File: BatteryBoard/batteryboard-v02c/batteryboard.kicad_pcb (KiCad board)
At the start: 4 copper layers, 95.9 x 90.2 mm, 40 parts, among them J1 KEYSTONE-1042, J2 KEYSTONE-1042, J3 KEYSTONE-1042, J4 KEYSTONE-1042, J5 KEYSTONE-1042, J6 KEYSTONE-1042, J7 MOLEX 502352-0801, J8 1985807, Q1 IRF7458, Q2 IRF7458, Q3 DMP2040USS-13, Q4 IRLML2803, U1 R5460N233AF

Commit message: changed flags
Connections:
- net PyCubed_AIN5 renamed PyCubed_SENSE
- net PyCubed_HIN renamed PyCubed_ENABLE
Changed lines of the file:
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@@
 	(net 6 "Net-(U1-VC)")
 	(net 7 "Net-(C3-Pad1)")
-	(net 8 "PyCubed_AIN5")
+	(net 8 "PyCubed_SENSE")
 	(net 9 "unconnected-(H1-Pad1)")
 	(net 10 "Net-(U1-V-)")
@@
 	(net 17 "Net-(Q2-G)")
 	(net 18 "/HEATER")
-	(net 19 "PyCubed_HIN")
+	(net 19 "PyCubed_ENABLE")
 	(net 20 "Net-(Q4-G)")
 	(net 21 "PYCUBED_GND")
@@
 			(layers "F.Cu" "F.Paste" "F.Mask")
 			(roundrect_rratio 0.25)
-			(net 8 "PyCubed_AIN5")
+			(net 8 "PyCubed_SENSE")
 			(pintype "passive")
 		)
@@
 			(layers "*.Cu" "*.Mask")
 			(remove_unused_layers no)
-			(net 8 "PyCubed_AIN5")
+			(net 8 "PyCubed_SENSE")
 			(pintype "passive")
 		)
@@
 			(layers "F.Cu" "F.Paste" "F.Mask")
 			(roundrect_rratio 0.25)
-			(net 19 "PyCubed_HIN")
+			(net 19 "PyCubed_ENABLE")
 			(pintype "passive")
 		)
@@
 			(size 1.2446 3.2512)
 			(layers "F.Cu" "F.Paste" "F.Mask")
-			(net 19 "PyCubed_HIN")
+			(net 19 "PyCubed_ENABLE")
 			(pinfunction "5")
 			(pintype "passive")
@@
 			(size 1.2446 3.2512)
 			(layers "F.Cu" "F.Paste" "F.Mask")
-			(net 8 "PyCubed_AIN5")
+			(net 8 "PyCubed_SENSE")
 			(pinfunction "6")
 			(pintype "passive")

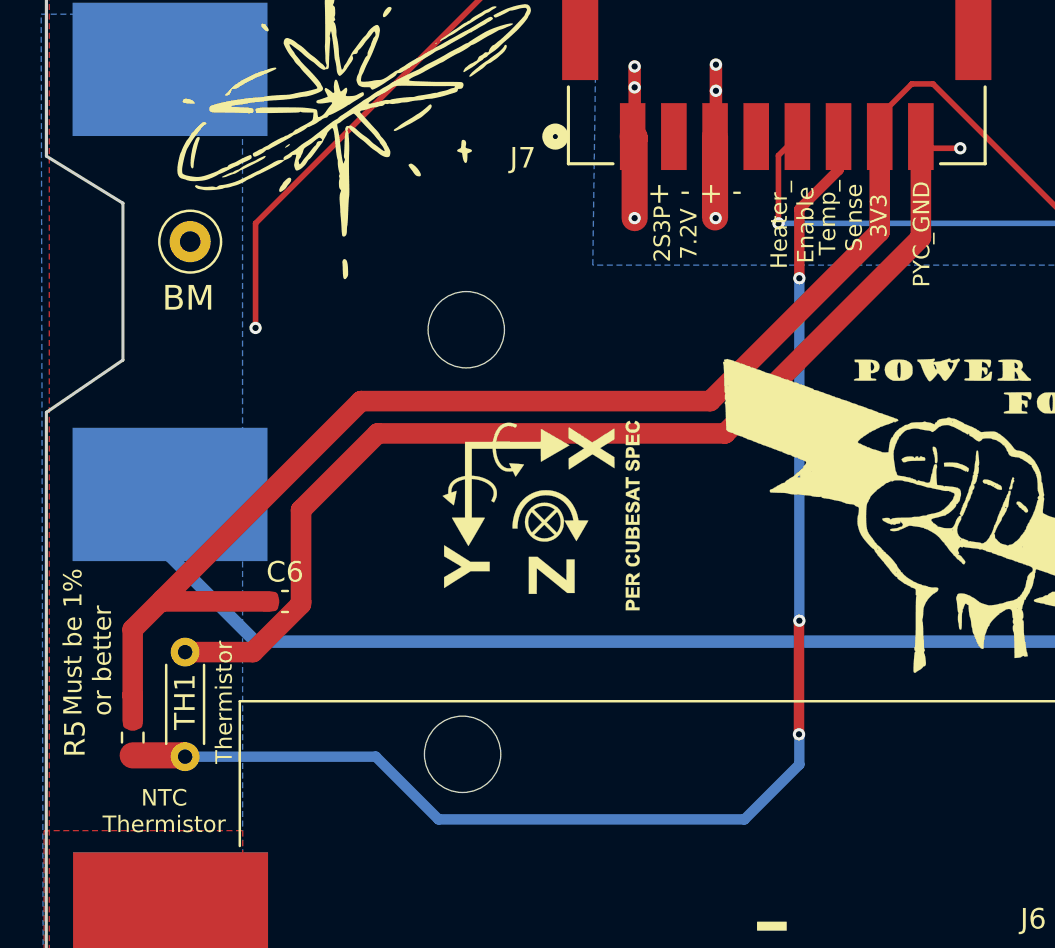
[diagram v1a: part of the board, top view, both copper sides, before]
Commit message: fixed traces on thermistor circuit
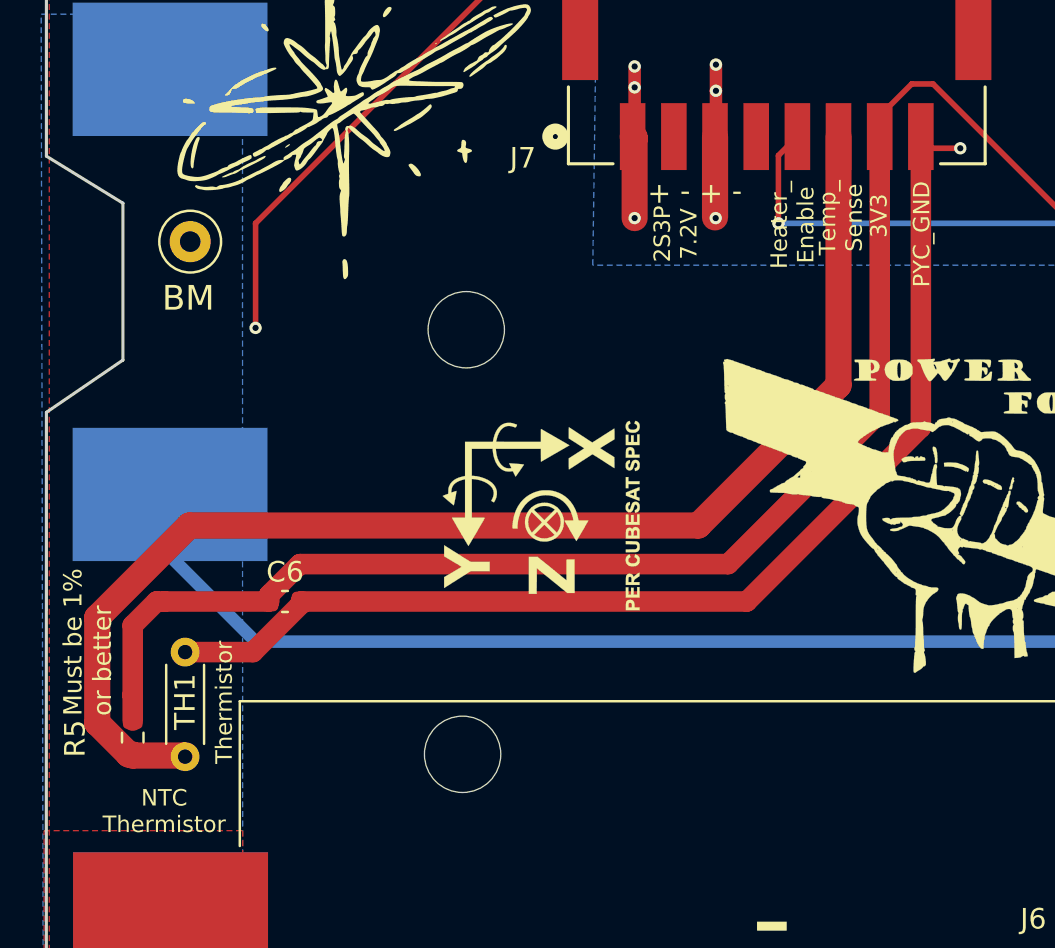
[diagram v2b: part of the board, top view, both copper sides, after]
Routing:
- net PYCUBED_GND: track 140.0 -> 142.8 mm
- net PyCubed_SENSE: track 65.6 -> 62.8 mm, vias 3 -> 0
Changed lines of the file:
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@@
 	(segment
 		(start 57.3913 101.2464)
-		(end 59.8778 101.2464)
+		(end 57.3988 101.2539)
 		(width 1.27)
 		(layer "F.Cu")
@@
 	)
 	(segment
-		(start 89.7763 74.715499)
-		(end 91.680299 72.8115)
-		(width 0.508)
+		(start 57.3988 101.2539)
+		(end 59.8853 101.2539)
+		(width 1.27)
 		(layer "F.Cu")
 		(net 8)
 	)
 	(segment
-		(start 59.8778 101.2464)
-		(end 59.9393 101.3079)
+		(start 91.680299 71.1859)
+		(end 91.680299 83.268301)
 		(width 1.27)
 		(layer "F.Cu")
@@
 	)
 	(segment
-		(start 91.680299 72.8115)
-		(end 91.680299 71.1859)
-		(width 0.508)
+		(start 59.8853 101.2539)
+		(end 59.9393 101.3079)
+		(width 1.27)
 		(layer "F.Cu")
 		(net 8)
 	)
 	(segment
-		(start 89.7599 94.7203)
-		(end 89.7763 94.7039)
-		(width 0.508)
+		(start 84.8697 90.0789)
+		(end 60.141876 90.0789)
+		(width 1.27)
 		(layer "F.Cu")
 		(net 8)
 	)
 	(segment
-		(start 89.7599 100.2215)
-		(end 89.7599 94.7203)
-		(width 0.508)
+		(start 55.6697 99.669914)
+		(end 57.203686 101.2039)
+		(width 1.27)
 		(layer "F.Cu")
 		(net 8)
 	)
 	(segment
-		(start 89.7763 78.0669)
-		(end 89.7763 74.715499)
-		(width 0.508)
+		(start 60.141876 90.0789)
+		(end 55.6697 94.551076)
+		(width 1.27)
 		(layer "F.Cu")
 		(net 8)
 	)
-	(via
-		(at 89.7763 78.0669)
-		(size 0.6)
-		(drill 0.3)
-		(layers "F.Cu" "B.Cu")
-		(net 8)
-	)
-	(via
-		(at 89.7599 100.2215)
-		(size 0.6)
-		(drill 0.3)
-		(layers "F.Cu" "B.Cu")
-		(net 8)
-	)
-	(via
-		(at 89.7763 94.7039)
-		(size 0.6)
-		(drill 0.3)
-		(layers "F.Cu" "B.Cu")
-		(net 8)
-	)
 	(segment
-		(start 89.7763 101.6889)
-		(end 89.7763 100.2379)
-		(width 0.508)
-		(layer "B.Cu")
-		(net 8)
-	)
-	(segment
-		(start 72.2503 104.3559)
-		(end 87.1093 104.3559)
-		(width 0.508)
-		(layer "B.Cu")
-		(net 8)
-	)
-	(segment
-		(start 69.2023 101.3079)
-		(end 72.2503 104.3559)
-		(width 0.508)
-		(layer "B.Cu")
-		(net 8)
-	)
-	(segment
-		(start 89.7763 94.7039)
-		(end 89.7763 78.0669)
-		(width 0.508)
-		(layer "B.Cu")
-		(net 8)
-	)
-	(segment
-		(start 60.4393 101.3079)
-		(end 69.2023 101.3079)
-		(width 0.508)
-		(layer "B.Cu")
+		(start 57.203686 101.2039)
+		(end 57.3947 101.2039)
+		(width 1.27)
+		(layer "F.Cu")
 		(net 8)
 	)
 	(segment
-		(start 89.7763 100.2379)
-		(end 89.7599 100.2215)
-		(width 0.508)
-		(layer "B.Cu")
+		(start 91.680299 83.268301)
+		(end 84.8697 90.0789)
+		(width 1.27)
+		(layer "F.Cu")
 		(net 8)
 	)
 	(segment
-		(start 87.1093 104.3559)
-		(end 89.7763 101.6889)
-		(width 0.508)
-		(layer "B.Cu")
+		(start 55.6697 94.551076)
+		(end 55.6697 99.669914)
+		(width 1.27)
+		(layer "F.Cu")
 		(net 8)
 	)
@@
 	)
 	(segment
-		(start 57.3947 98.3248)
-		(end 57.3947 99.5539)
-		(width 1)
-		(layer "F.Cu")
-		(net 15)
-	)
-	(segment
 		(start 109.68021 76.84999)
 		(end 111.36012 78.5299)
@@
 	)
 	(segment
-		(start 57.3913 98.3214)
-		(end 57.3913 95.1251)
+		(start 65.5197 91.9539)
+		(end 86.3197 91.9539)
 		(width 1)
 		(layer "F.Cu")
@@
 	)
 	(segment
-		(start 57.3913 98.3214)
-		(end 57.3947 98.3248)
+		(start 57.3947 98.3248)
+		(end 57.3913 98.3214)
+		(width 1)
+		(layer "F.Cu")
+		(net 15)
+	)
+	(segment
+		(start 64.0167 93.4569)
+		(end 65.5197 91.9539)
 		(width 1)
 		(layer "F.Cu")
@@
 	)
 	(segment
-		(start 109.68021 76.84999)
-		(end 111.6103 74.9199)
-		(width 0.27178)
+		(start 58.5537 93.7699)
+		(end 58.9497 93.7699)
+		(width 1)
 		(layer "F.Cu")
 		(net 15)
 	)
 	(segment
-		(start 93.6803 75.8033)
-		(end 93.6803 71.1859)
+		(start 86.3197 91.9539)
+		(end 93.6803 84.5933)
 		(width 1)
 		(layer "F.Cu")
@@
 	)
 	(segment
-		(start 57.3913 95.1251)
-		(end 58.8481 93.6683)
-		(width 1)
+		(start 109.68021 76.84999)
+		(end 111.6103 74.9199)
+		(width 0.27178)
 		(layer "F.Cu")
 		(net 15)
@@
 	)
 	(segment
+		(start 93.6803 84.5933)
+		(end 93.6803 71.1859)
+		(width 1)
+		(layer "F.Cu")
+		(net 15)
+	)
+	(segment
+		(start 57.3947 99.5539)
+		(end 57.3947 98.3248)
+		(width 1)
+		(layer "F.Cu")
+		(net 15)
+	)
+	(segment
 		(start 93.6803 71.1859)
 		(end 93.6803 70.1826)
@@
 	)
 	(segment
-		(start 85.4477 84.0359)
-		(end 93.6803 75.8033)
+		(start 57.3913 94.9323)
+		(end 58.5537 93.7699)
+		(width 1)
+		(layer "F.Cu")
+		(net 15)
+	)
+	(segment
+		(start 64.0167 93.7699)
+		(end 64.0167 93.4569)
+		(width 1)
+		(layer "F.Cu")
+		(net 15)
+	)
+	(segment
+		(start 57.3913 98.3214)
+		(end 57.3913 94.9323)
 		(width 1)
 		(layer "F.Cu")
@@
 	)
 	(segment
-		(start 58.8481 93.6683)
-		(end 68.4805 84.0359)
-		(width 1)
-		(layer "F.Cu")
-		(net 15)
-	)
-	(segment
-		(start 68.4805 84.0359)
-		(end 85.4477 84.0359)
-		(width 1)
-		(layer "F.Cu")
-		(net 15)
-	)
-	(segment
 		(start 111.5695 90.2539)
 		(end 111.5695 87.6935)
@@
 	)
 	(segment
-		(start 65.5697 93.7669)
-		(end 65.5697 89.3289)
+		(start 65.5667 93.7699)
+		(end 87.2287 93.7699)
 		(width 1)
 		(layer "F.Cu")
@@
 	)
 	(segment
-		(start 69.2947 85.6039)
-		(end 86.1697 85.6039)
-		(width 1)
-		(layer "F.Cu")
-		(net 21)
-	)
-	(segment
 		(start 115.9446 75.0349)
 		(end 115.351184 75.0349)
@@
 	)
 	(segment
-		(start 65.5667 93.7699)
-		(end 65.5697 93.7669)
+		(start 95.680301 85.318299)
+		(end 95.680301 71.1859)
 		(width 1)
 		(layer "F.Cu")
@@
 	)
 	(segment
+		(start 87.2287 93.7699)
+		(end 95.680301 85.318299)
+		(width 1)
+		(layer "F.Cu")
+		(net 21)
+	)
+	(segment
 		(start 115.9447 76.3539)
 		(end 115.9446 76.354)
@@
 	)
 	(segment
-		(start 95.680301 76.093299)
-		(end 95.680301 71.1859)
-		(width 1)
-		(layer "F.Cu")
-		(net 21)
-	)
-	(segment
 		(start 112.7947 71.7789)
 		(end 112.7697 71.7789)
@@
 	)
 	(segment
-		(start 86.1697 85.6039)
-		(end 95.680301 76.093299)
-		(width 1)
-		(layer "F.Cu")
-		(net 21)
-	)
-	(segment
 		(start 114.427894 74.11161)
 		(end 114.427894 73.437094)
@@
 		(layer "F.Cu")
 		(net 21)
-	)
-	(segment
-		(start 65.5697 89.3289)
-		(end 69.2947 85.6039)
-		(width 1)
-		(layer "F.Cu")
-		(net 21)
